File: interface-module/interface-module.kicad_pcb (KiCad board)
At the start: 2 copper layers, 71.6 x 79.1 mm, 96 parts, among them J1 Conn_01x02, J2 Conn_01x02, J4 Conn_01x08, J6 Conn_01x08, Q1 PMOS, Q10 NMOS, Q11 PMOS, Q12 NMOS, Q13 PMOS, Q14 NMOS, Q15 PMOS, Q16 NMOS, Q2 NMOS, Q3 PMOS, Q4 NMOS, Q5 PMOS, Q6 NMOS, Q7 PMOS, Q8 NMOS, Q9 PMOS, SW1 SW_Coded_SH-7050, U10 TCA9548, U11 MCP3464, U2 140357145200, U3 140357145200, U4 140357145200, U5 140357145200, U6 140357145200, U7 140357145200, U8 140357145200, U9 140357145200

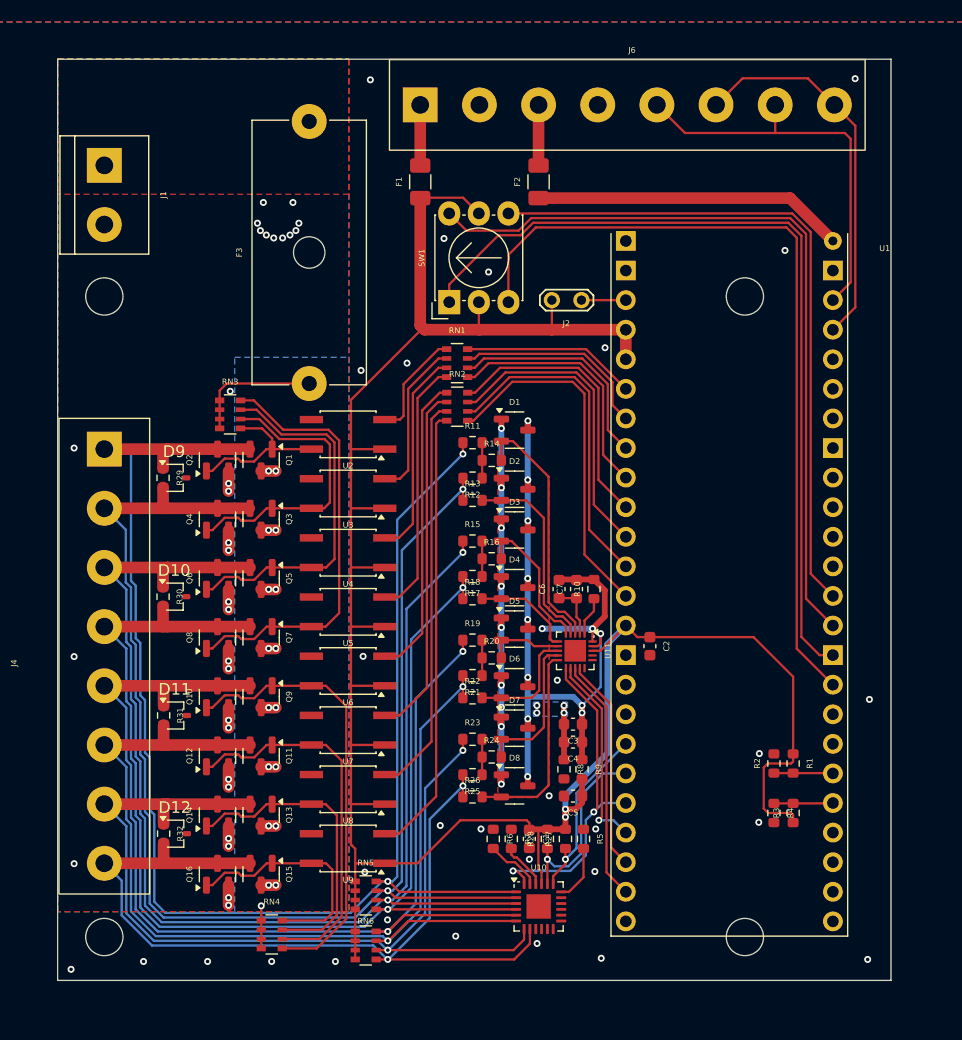
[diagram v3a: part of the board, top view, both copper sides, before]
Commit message: Updated silkscreen
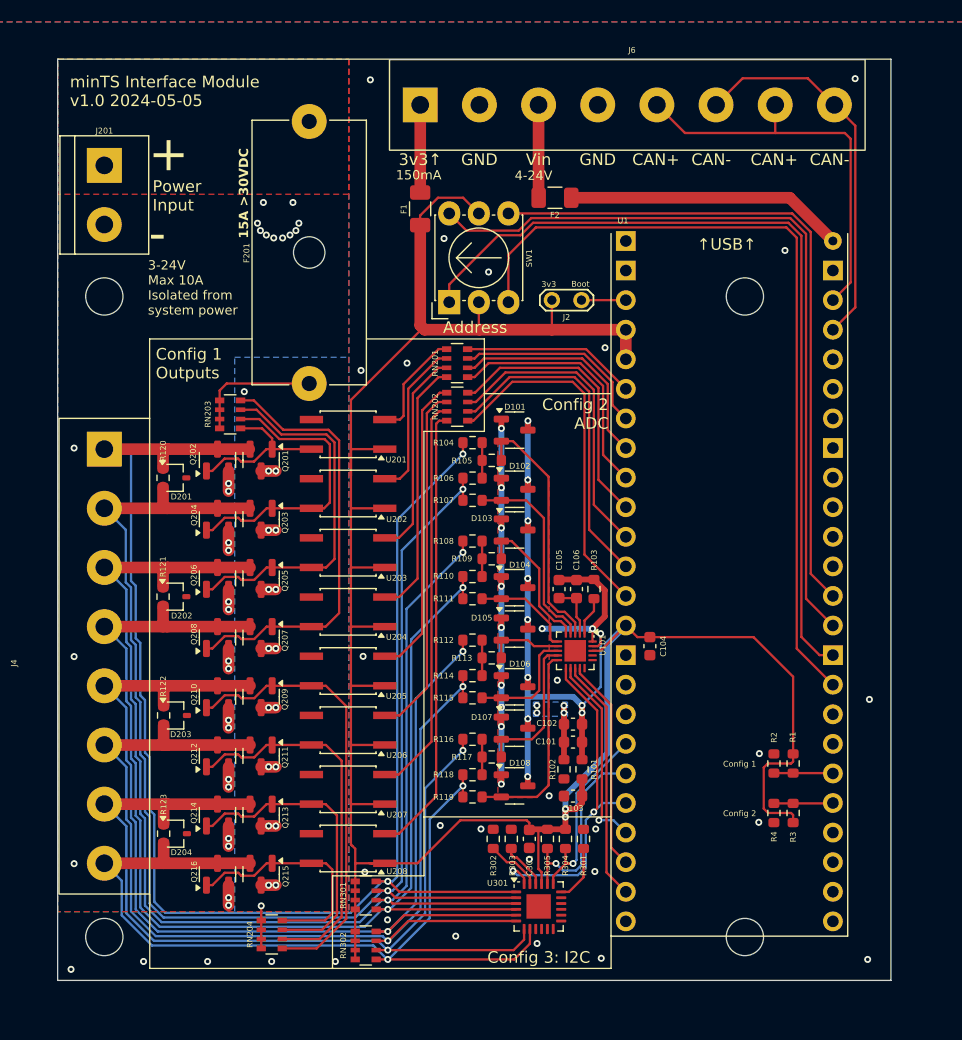
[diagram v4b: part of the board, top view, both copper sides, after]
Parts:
- moved F1 2.32 mm to (167.1, 26.4)
- moved F2 1.96 mm to (178.7, 25.5), turned to 180 degrees
- renumbered C4 to C101, C3 to C102, C5 to C103, C2 to C104, C6 to C105, C7 to C106, C1 to C301, D1 to D101, D2 to D102, D3 to D103, D4 to D104, D5 to D105, D6 to D106, D7 to D107, D8 to D108, D9 to D201, D10 to D202, D11 to D203, D12 to D204, F3 to F201, J1 to J201, Q1 to Q201, Q2 to Q202, Q3 to Q203, Q4 to Q204, Q5 to Q205, Q6 to Q206, Q7 to Q207, Q8 to Q208, Q9 to Q209, Q10 to Q210, Q11 to Q211, Q12 to Q212, Q13 to Q213, Q14 to Q214, Q15 to Q215, Q16 to Q216, R9 to R101, R8 to R102, R10 to R103, R11 to R104, R14 to R105, R12 to R106, R13 to R107, R15 to R108, R16 to R109, R17 to R110, R18 to R111, R19 to R112, R20 to R113, R21 to R114, R22 to R115, R23 to R116, R24 to R117, R25 to R118, R26 to R119, R29 to R120, R30 to R121, R31 to R122, R32 to R123, R5 to R301, R6 to R302, R7 to R303, R27 to R304, R28 to R305, RN1 to RN201, RN2 to RN202, RN3 to RN203, RN4 to RN204, RN5 to RN301, RN6 to RN302, U11 to U101, U2 to U201, U3 to U202, U4 to U203, U5 to U204, U6 to U205, U7 to U206, U8 to U207, U9 to U208, U10 to U301
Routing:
- net VBUS: track 26.8 -> 24.0 mm
- net Net-(J6-Pin_3): track 5.20 -> 7.98 mm
- net Net-(J6-Pin_1): track 5.20 -> 7.53 mm
- net I2C_SCL: track 15.5 -> 16.9 mm
- net CTRL: track 29.3 -> 30.2 mm
- net +3V3: track 210.7 -> 209.8 mm
- net I2C_SDA: track 16.3 -> 17.0 mm
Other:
- board text added: "${TITLE} ${REVISION} ${ISSUE_DATE}"
- board text added: "+"
- board text added: "-"
- board text added: "150mA"
- board text added: "15A >30VDC"
- board text added: "3-24V Max 10A Isolated from system power"
- board text added: "3v3"
- board text added: "3v3↑"
- board text added: "4-24V"
- board text added: "Address"
- board text added: "Boot"
- board text added: "CAN+"
- board text added: "CAN-"
- board text added: "Config 1"
- board text added: "Config 1 Outputs"
- board text added: "Config 2"
- board text added: "Config 2 ADC"
- board text added: "Config 3: I2C"
- board text added: "GND"
- board text added: "Power Input"
- board text added: "Vin"
- board text added: "↑USB↑"

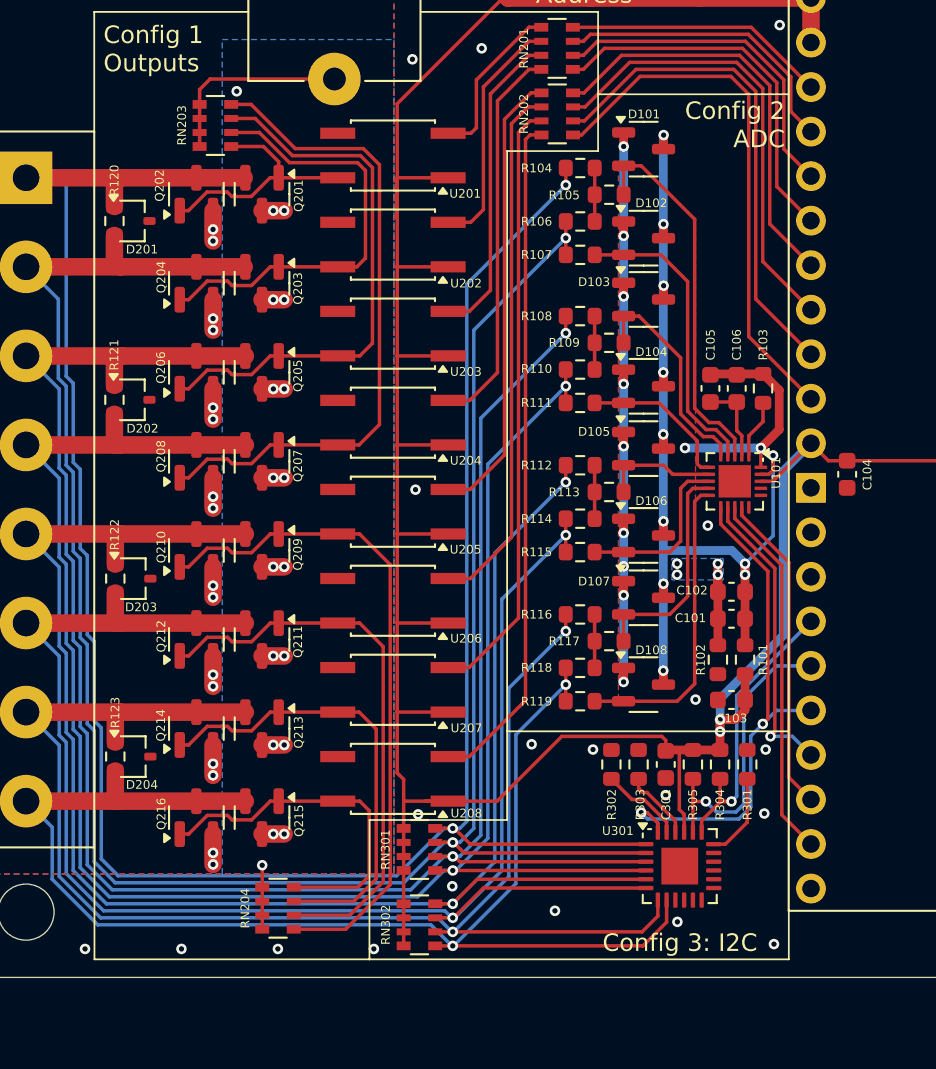
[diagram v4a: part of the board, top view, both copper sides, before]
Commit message: Exported devboard STEP
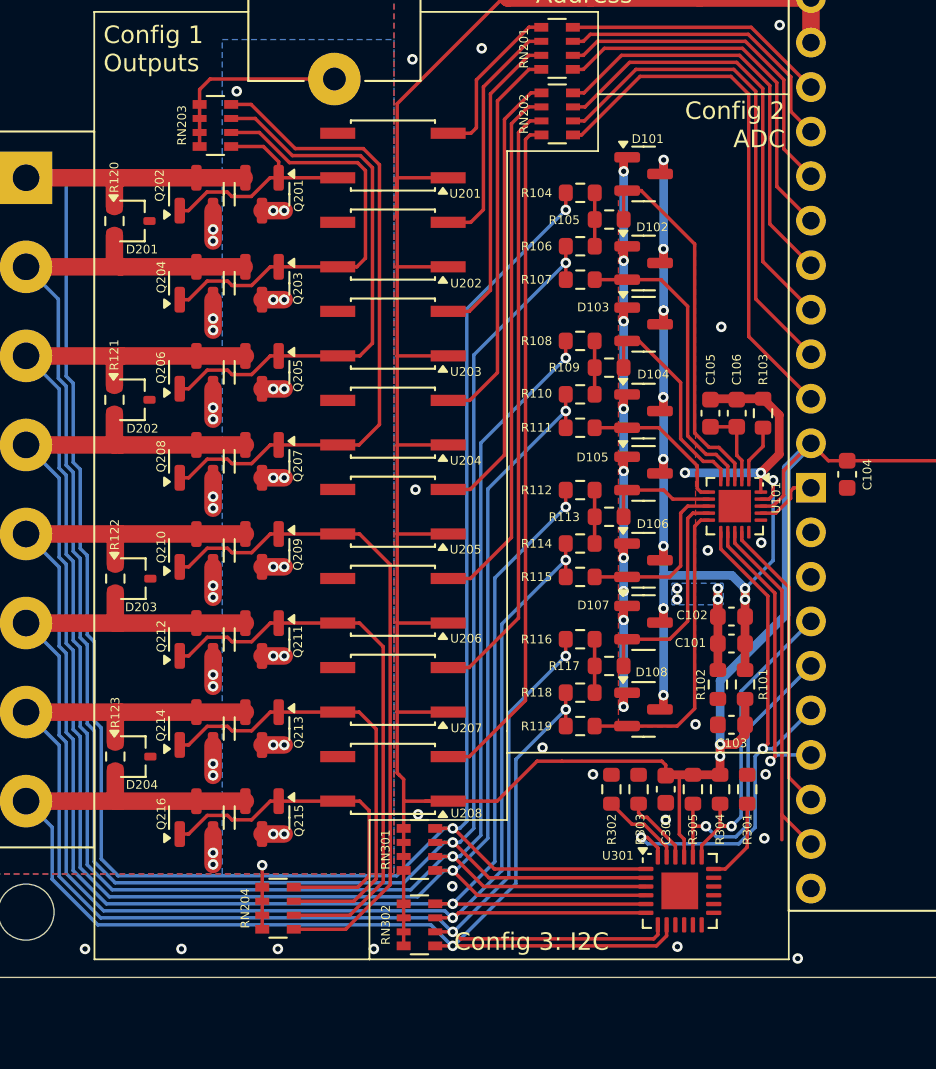
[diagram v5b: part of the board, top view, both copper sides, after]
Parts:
- D101, D102, D103, D104, D105, D106, D107, D108: footprint Package_TO_SOT_SMD:SOT-23-3 -> Package_TO_SOT_SMD:SOT-23
- moved C101 1.42 mm to (180.2, 73.7)
- moved C103 1.42 mm to (180.2, 78.3)
- moved C301 1.42 mm to (176.5, 82.0)
- moved D106 1.42 mm to (175.2, 68.9)
- moved D108 1.42 mm to (175.2, 77.4)
- moved R107 1.42 mm to (171.6, 52.9)
- moved R111 1.42 mm to (171.6, 61.3)
- moved R113 1.42 mm to (173.3, 66.4)
- moved R114 1.42 mm to (171.6, 67.9)
- moved R115 1.42 mm to (171.6, 69.9)
- moved R116 1.42 mm to (171.6, 73.4)
- moved R117 1.42 mm to (173.3, 74.9)
- moved R118 1.42 mm to (171.6, 76.5)
- moved R119 1.42 mm to (171.6, 78.4)
- moved R301 1.42 mm to (181.2, 82.0)
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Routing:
- net GND: track 0.00 -> 4.71 mm, vias 30 -> 31
- net OUT7/IN3-: track 78.3 -> 75.9 mm
- net +3V3: track 209.8 -> 212.1 mm
- net OUT5/IN2-: track 91.7 -> 89.7 mm
- net OUT4/IN2+: track 97.3 -> 95.3 mm
- net OUT6/IN3+: track 82.9 -> 81.0 mm
- net I2C_SCL: track 16.9 -> 18.3 mm
- net SPI_MISO: track 18.3 -> 16.9 mm
- net OUT1/IN0-: track 123.3 -> 122.4 mm
- net OUT0/IN0+: track 130.4 -> 129.5 mm
- net OUT3/IN1-: track 106.5 -> 105.7 mm
- net OUT2/IN1+: track 112.8 -> 112.0 mm

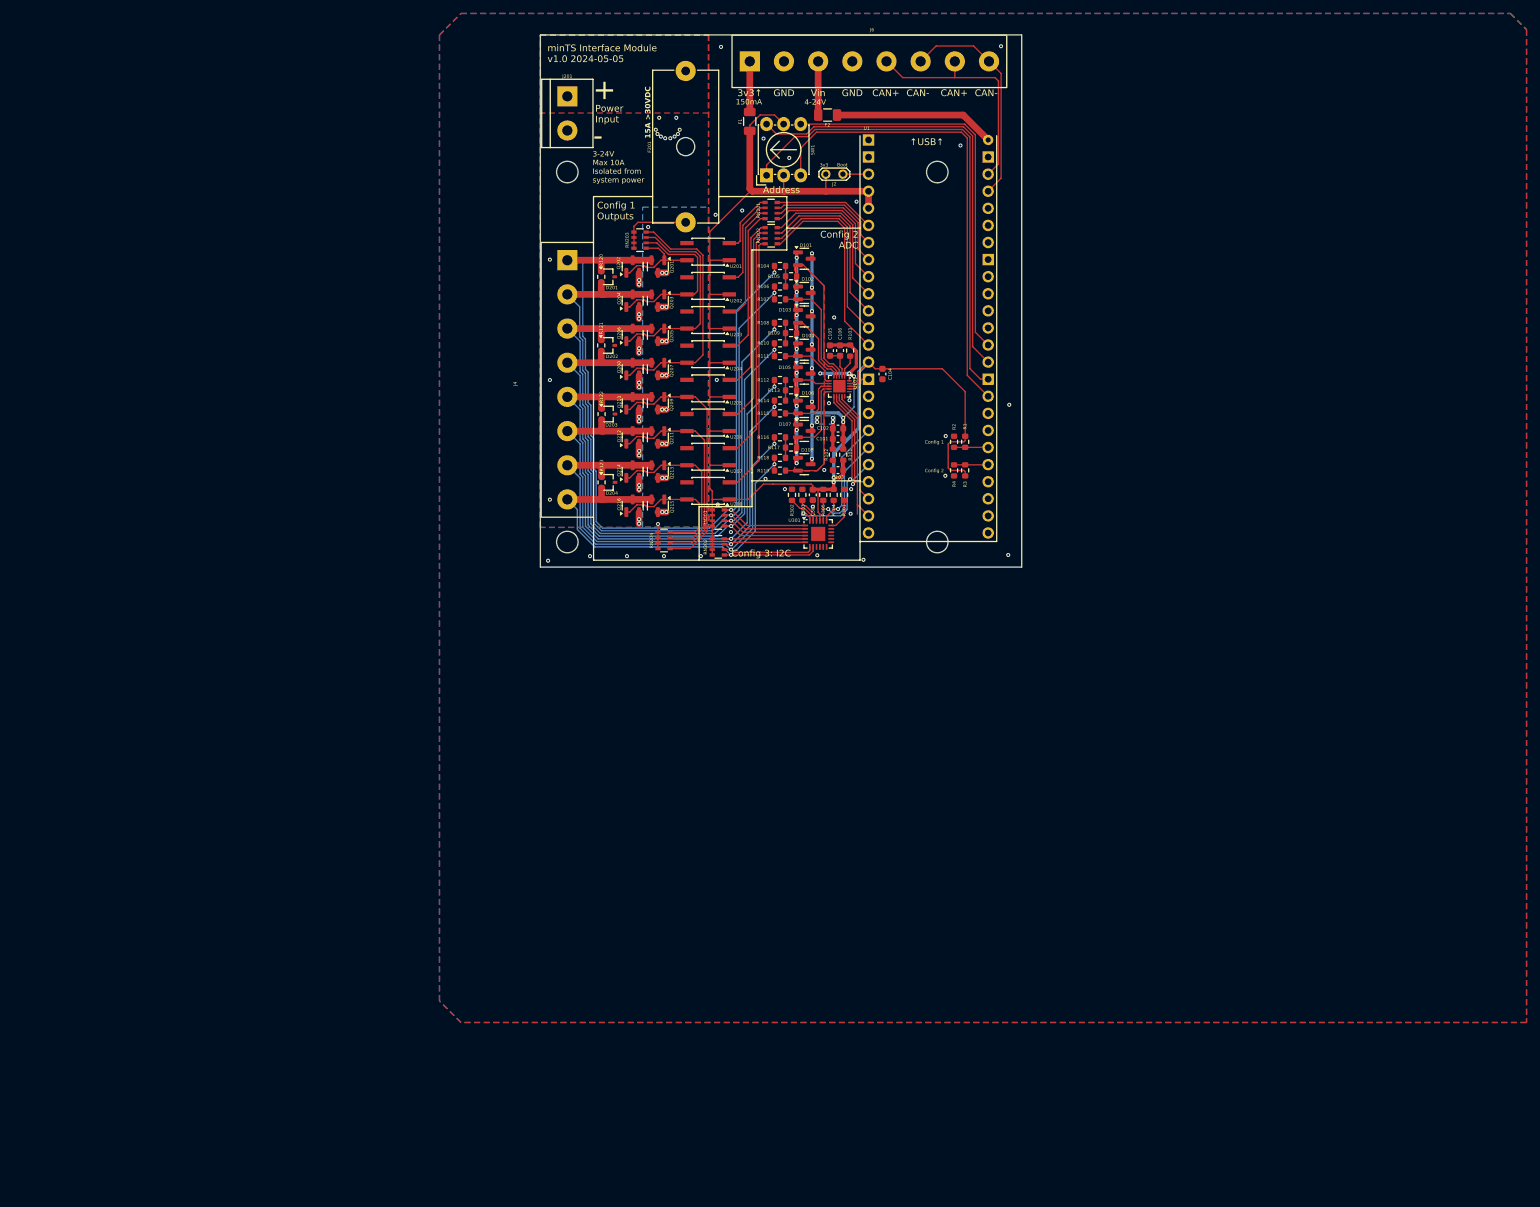
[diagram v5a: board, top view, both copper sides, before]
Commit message: More silkscreen and fixing some footprints
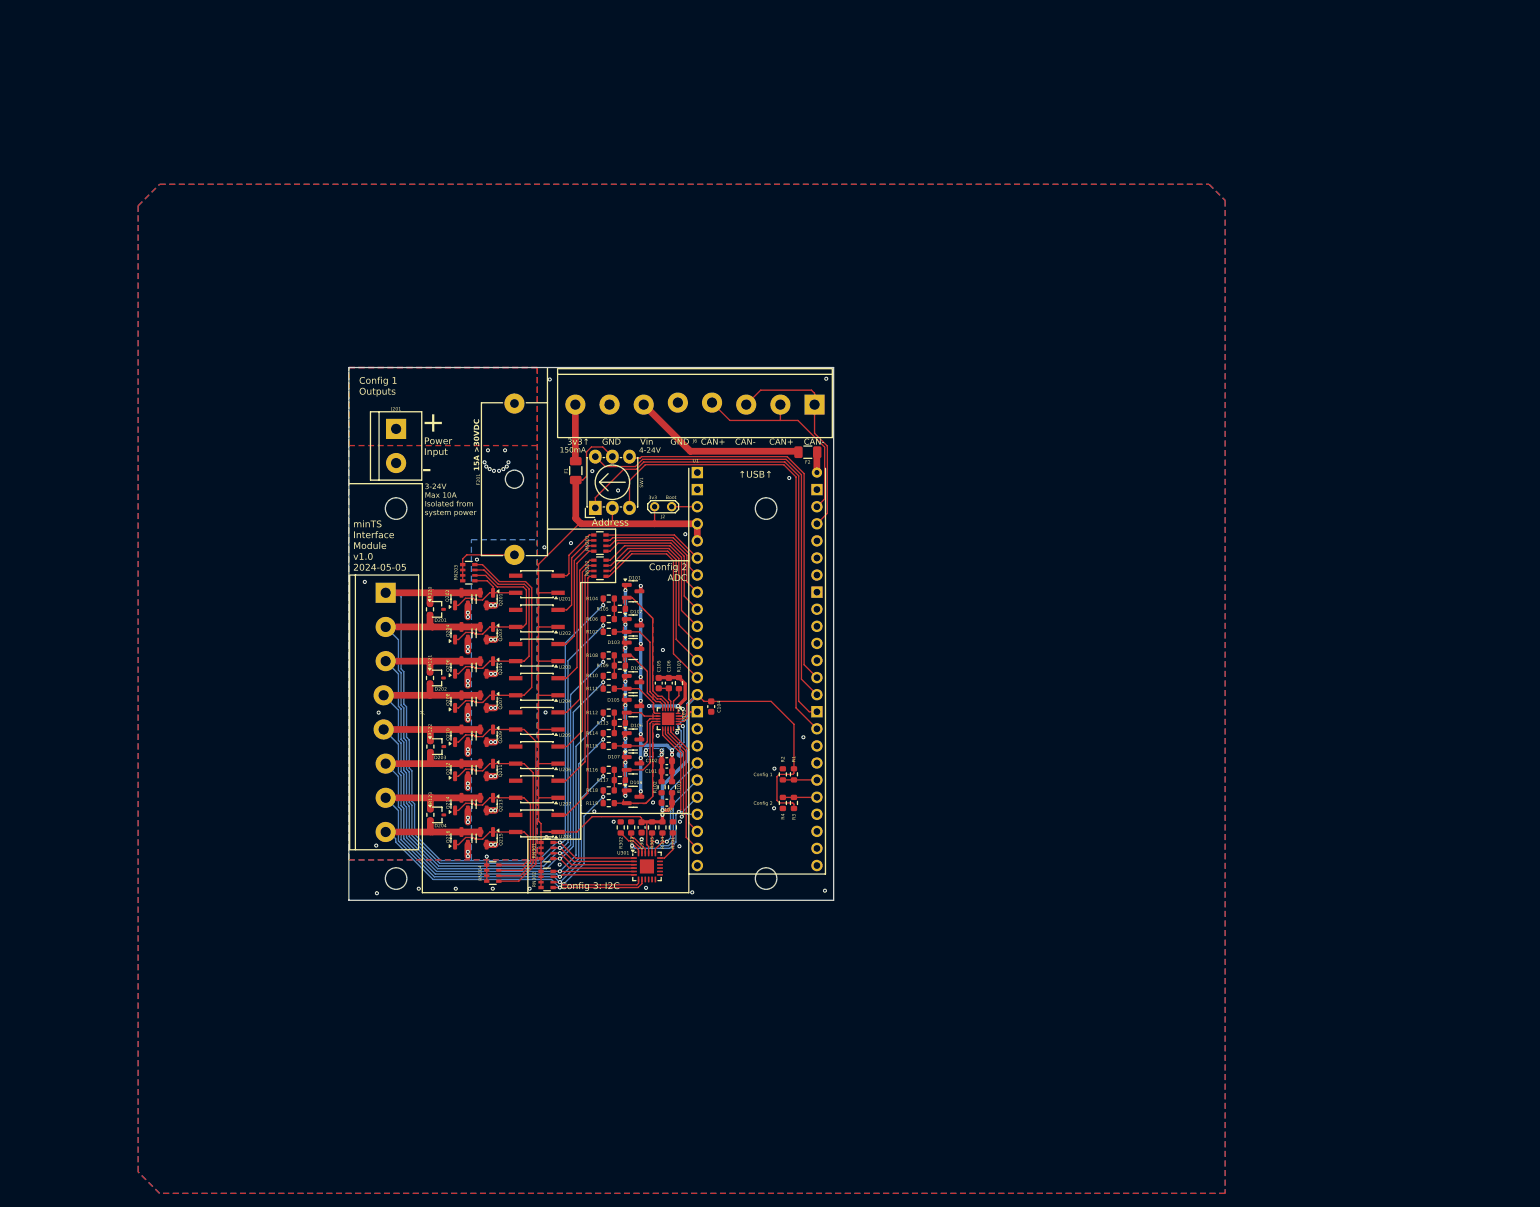
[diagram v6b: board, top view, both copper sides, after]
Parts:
- added TP201: TestPoint, TestPoint:TestPoint_Pad_D1.0mm, B.Cu at (156.8, 120.6)
- J4, J6: footprint TerminalBlock:TerminalBlock_bornier-8_P5.08mm -> footprints:TerminalBlock_CUI-8_P5.08mm
- moved F1 58.0 mm to (141.3, 78.4)
- moved J4 56.3 mm to (113.0, 96.5)
- moved REF** 56.1 mm to (169.6, 139.0)
- moved REF** 56.1 mm to (114.6, 139.0)
- moved REF** 56.1 mm to (114.6, 84.0)
- moved REF** 56.1 mm to (169.6, 84.0)
- moved Q215 55.6 mm to (128.0, 133.0)
- moved RN204 55.6 mm to (128.9, 138.2)
- moved C101 55.6 mm to (154.8, 123.1)
- moved C102 55.6 mm to (154.8, 121.6)
- moved C104 55.6 mm to (161.4, 113.4)
- moved C105 55.6 mm to (153.6, 110.0)
- moved C106 55.6 mm to (155.1, 110.0)
- moved C301 55.6 mm to (151.0, 131.4)
- moved D103 55.6 mm to (149.8, 104.9)
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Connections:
- F1 pad 2: Net-(J6-Pin_1) -> Net-(J6-Pin_8)
- F2 pad 2: Net-(J6-Pin_3) -> Net-(J6-Pin_6)
- J6 pad 1: Net-(J6-Pin_1) -> CAN-
- J6 pad 2: GND -> CAN+
- J6 pad 3: Net-(J6-Pin_3) -> CAN-
- J6 pad 4: GND -> CAN+
- J6 pad 5: CAN+ -> GND
- J6 pad 6: CAN- -> Net-(J6-Pin_6)
- J6 pad 7: CAN+ -> GND
- J6 pad 8: CAN- -> Net-(J6-Pin_8)
- U101 pad 16: unconnected-(U101-MCLK-Pad16) -> Net-(U101-MCLK)
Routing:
- net Net-(J6-Pin_6): track 0.00 -> 25.9 mm
- net VBUS: track 24.0 -> 3.05 mm
- net Net-(J6-Pin_8): track 0.00 -> 8.43 mm
- net Net-(J6-Pin_3): track 7.98 -> 0.00 mm
- net Net-(J6-Pin_1): track 7.53 -> 0.00 mm
- net Net-(U101-MCLK): track 0.00 -> 5.43 mm, vias 0 -> 1
- net CAN+: track 34.7 -> 31.2 mm
- net OUT4/IN2+: track 95.3 -> 97.1 mm
- net OUT3/IN1-: track 105.7 -> 107.5 mm
- net SPI_MOSI: track 21.0 -> 19.6 mm
- net +3V3: track 212.1 -> 212.9 mm
- net CAN-: track 32.9 -> 32.1 mm
- net Net-(U1-PA6): track 66.8 -> 66.3 mm
- net Net-(U1-PA5): track 72.2 -> 71.7 mm
- net Net-(U1-PA4): track 69.8 -> 69.3 mm
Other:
- board size 71.6 x 79.1 mm -> 72.1 x 79.2 mm
- board text added: "1: ADC"
- board text added: "2: OUT"
- board text added: "3: I2C"
- board text added: "ADC MCLK"
- board text added: "Configured as"
- board text added: "S/N"
- board text added: "See GitHub for info"
- board text added: "github.com/psas/ mints-scada-hardware"
- board text added: "minTS Interface Module ${REVISION} ${ISSUE_DATE}"
- board text removed: "${TITLE} ${REVISION} ${ISSUE_DATE}"
